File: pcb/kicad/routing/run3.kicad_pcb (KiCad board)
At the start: 4 copper layers, 150 x 100 mm, 150 parts, among them J1 SWD, J2 USB4085-GF-A, J3 LiPo JST-PH 2.0mm (1 = + RED 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, J4 LCD 1.54in ST7789 module, JST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, J5 Speaker JST-PH, J6 microSD Molex 104031-0811, J7 STEMMA QT, J8 Expansion (6 = VBAT_SENSE ADC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, J9 LCD header 2.54 mm (wire by n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, Q1 FS8205A, Q3 AO3400A, Q4 AO3401A, Q6 AO3401A (DNP: fit only for a 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, SW1 BOOT, SW10 DPAD LEFT PTS645SM43SMTR92, SW11 DPAD RIGHT PTS645SM43SMTR92, SW12 DPAD PRESS PTS645SM43SMTR92, SW2 RESET, SW3 POWER PCM12, SW4 A PTS125SM43SMTR2LFS, SW5 B PTS125SM43SMTR2LFS, SW6 X PTS125SM43SMTR2LFS, SW7 Y PTS125SM43SMTR2LFS, SW8 DPAD UP PTS645SM43SMTR92, SW9 DPAD DOWN PTS645SM43SMTR92, U1 RP2350A, U10 LSM6DSOXTR, U11 RM2, U2 W25Q128JVSIQ, U3 APS6404L-3SQR-SN, U4 USBLC6-2SC6, U5 BQ24074RGTR, U6 TPS63001DRCR, U7 DW01A, U8 PAM8302AADCR, U9 DS3231MZ+, Y1 12MHz ABM8-272-T3

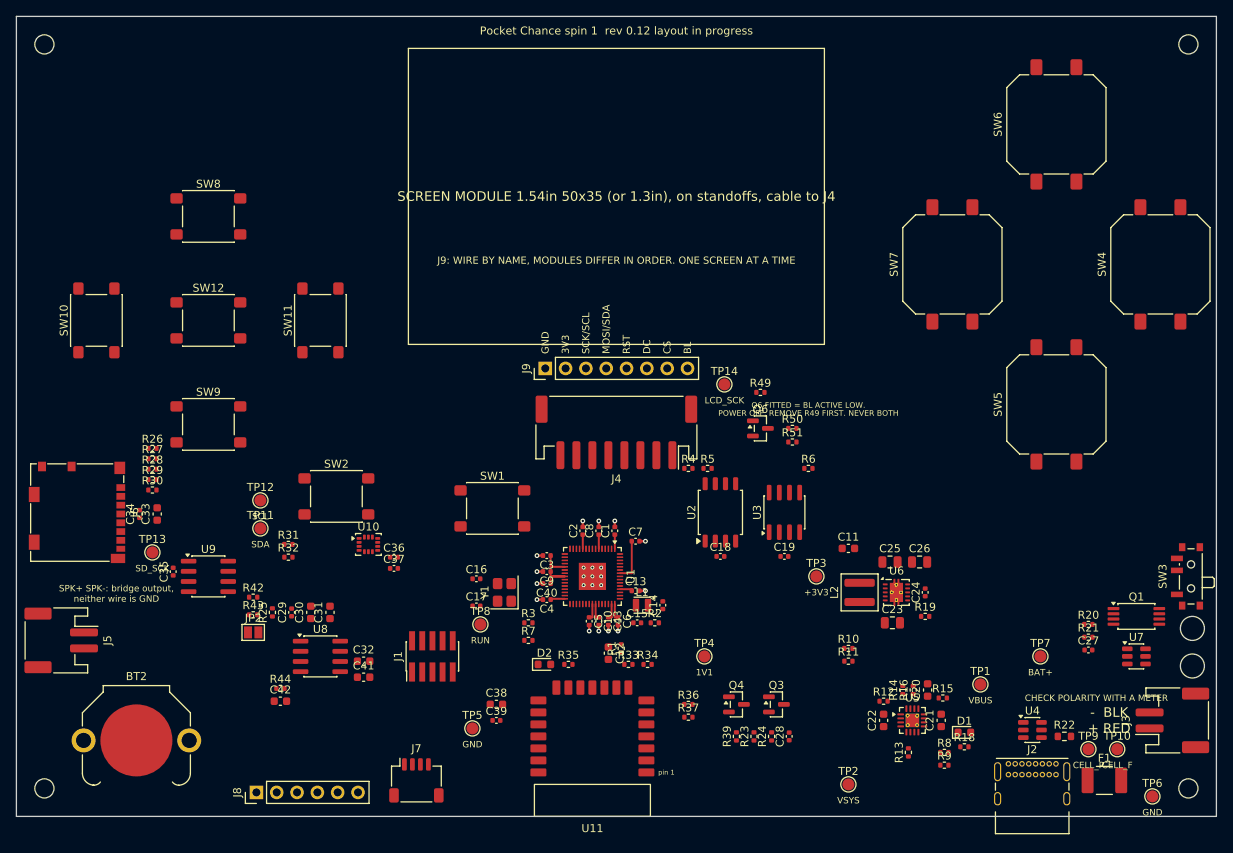
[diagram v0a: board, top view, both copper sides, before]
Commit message: Routing run 3 (NOT FOR FAB): Freerouting around the straightened stage-1 stubs: 7 unrouted (run 1: 8, run 2: 13)
Input: rev 0.12 board with stage 1 (4c0a832), In1 GND / In2 +3V3 planes, 25 passes. Imported: 1282
segments, 229 vias. DRC: 0 clearance errors, 2 tracks necked to 0.12 mm, 7 unrouted, all at U1.

Co-Authored-By: Claude Opus 5.5 <noreply@anthropic.com>
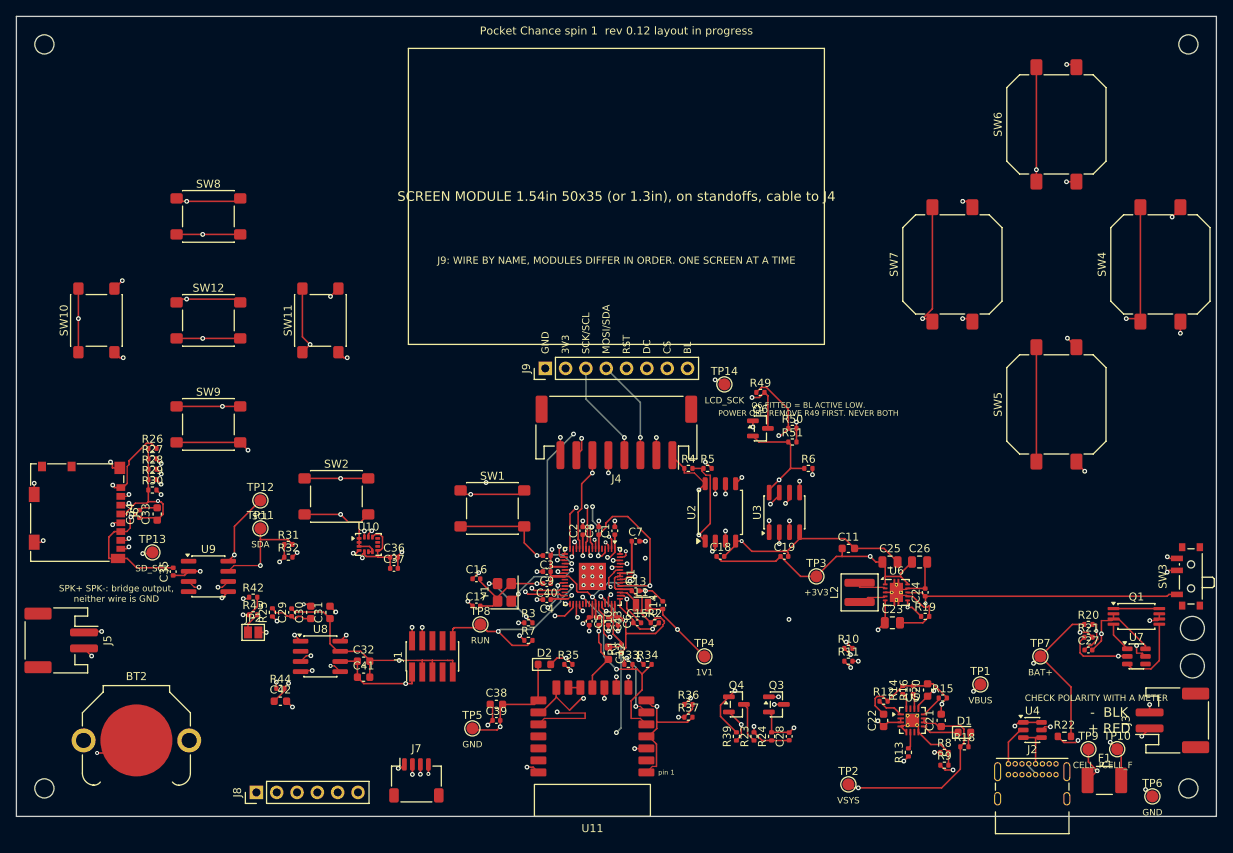
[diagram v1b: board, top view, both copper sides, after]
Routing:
- net GND: track 9.75 -> 297.9 mm, vias 22 -> 60
- net +3V3: track 19.9 -> 165.1 mm, vias 0 -> 21
- net SDA: track 0.00 -> 112.9 mm, vias 0 -> 4
- net BTN_A: track 0.00 -> 111.9 mm, vias 0 -> 3
- net SCL: track 0.00 -> 111.5 mm, vias 0 -> 5
- net BTN_X: track 0.00 -> 99.2 mm, vias 0 -> 3
- net VSYS: track 0.00 -> 93.3 mm, vias 0 -> 3
- net BTN_Y: track 0.00 -> 89.2 mm, vias 0 -> 3
- net JOY_UP: track 0.00 -> 83.0 mm, vias 0 -> 4
- net JOY_LEFT: track 0.00 -> 82.9 mm, vias 0 -> 2
- net VBAT_SENSE: track 0.00 -> 78.0 mm, vias 0 -> 3
- net VBUS: track 0.00 -> 77.7 mm, vias 0 -> 5
- net SD_CS: track 0.00 -> 74.1 mm, vias 0 -> 3
- net SD_MISO: track 0.00 -> 68.6 mm, vias 0 -> 3
- net SD_MOSI: track 0.00 -> 68.4 mm, vias 0 -> 3
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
